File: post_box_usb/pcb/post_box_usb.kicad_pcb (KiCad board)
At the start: 4 copper layers, 92.9 x 45 mm, 114 parts, among them U1 MCP1700T-3302E/MB, U2 PMV65XP,215, X1 MC146 32768Hz

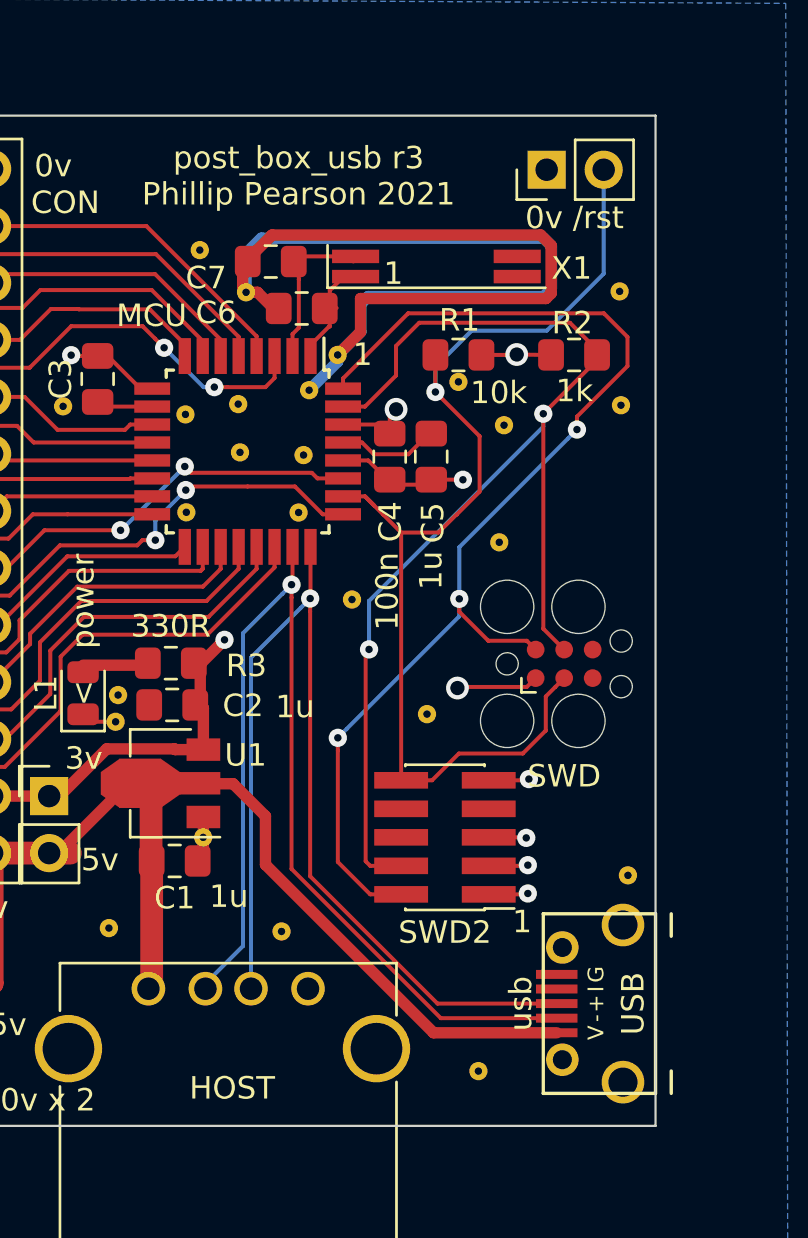
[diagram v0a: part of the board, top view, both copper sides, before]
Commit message: post_box_usb: Start r4; generate JLCPCB BOM so I can get them to assemble these.
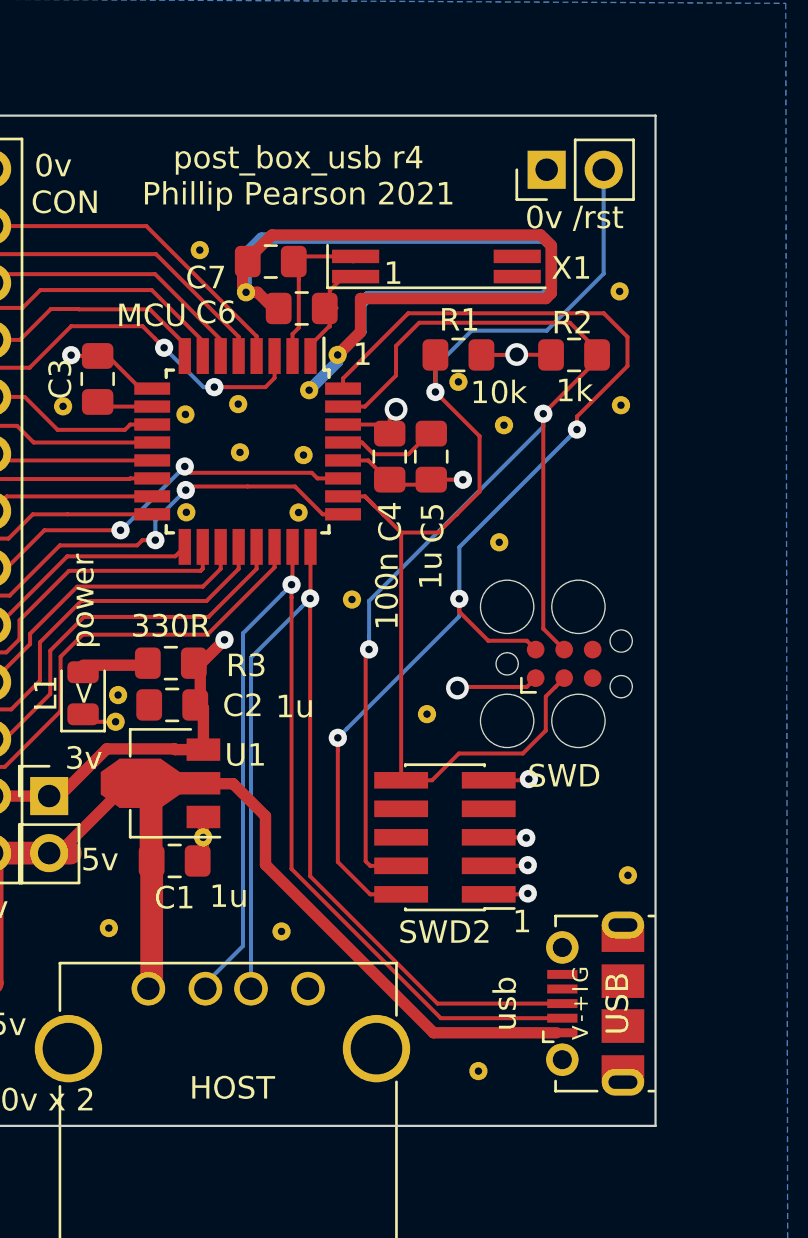
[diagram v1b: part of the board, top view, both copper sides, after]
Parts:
- C6, C7: value 15p -> NF 15p
- CON, FPGA_IO, FPGA_IO2, TEST: value pins -> NF pins
- FPGA_JTAG: value lattice jtag -> NF lattice jtag
- HOST: value usb host -> NF usb host
- PWR: value reset -> NF power
- R18, R19: value 0R NF -> NF 0R
- RST: value reset -> NF reset
- USB: footprint myelin-kicad:micro_usb_b_smd_molex -> Connector_USB:USB_Micro-B_Molex-105017-0001
- X1: value MC146 32768Hz -> NF MC146 32768Hz
- moved USB 0.69 mm to (197.3, 169.6)
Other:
- board text added: "post_box_usb r4 Copyright 2017-2021 Google Inc Designed by Phillip Pearson myelin.nz/acorn/postbox"
- board text added: "post_box_usb r4 Phillip Pearson 2021"
- board text removed: "post_box_usb r3 Copyright 2017-2021 Google Inc Designed by Phillip Pearson myelin.nz/acorn/postbox"
- board text removed: "post_box_usb r3 Phillip Pearson 2021"

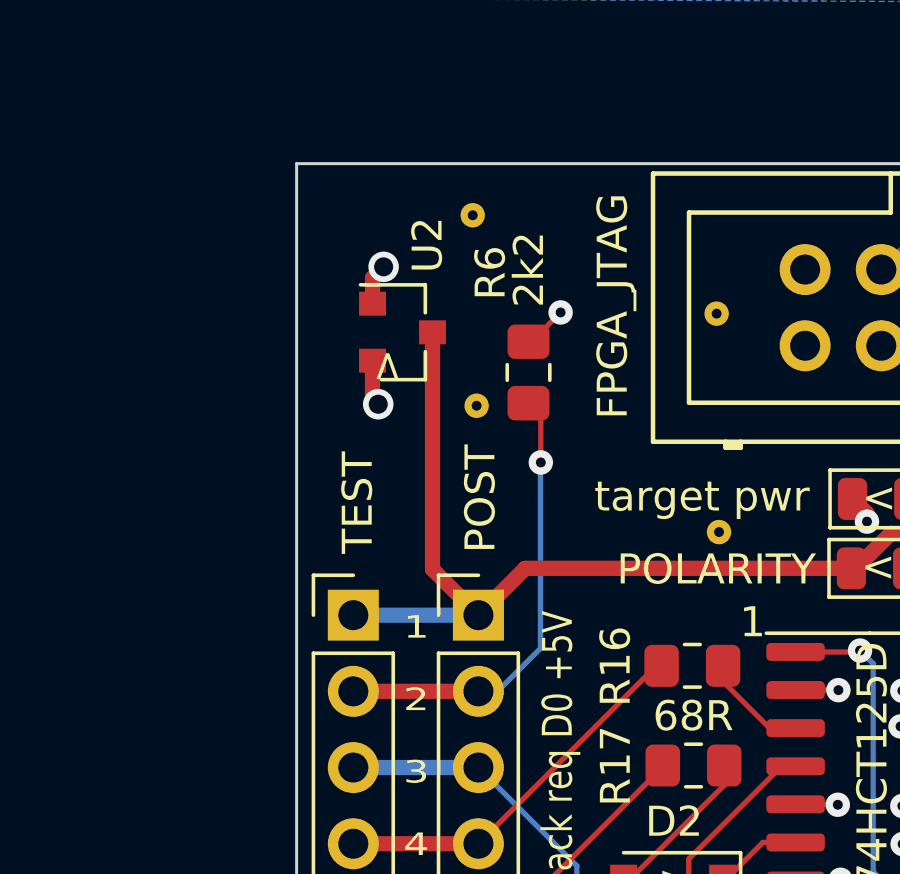
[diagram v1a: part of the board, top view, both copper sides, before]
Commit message: post_box_usb: add two pulldown resistors for target_5V_ext
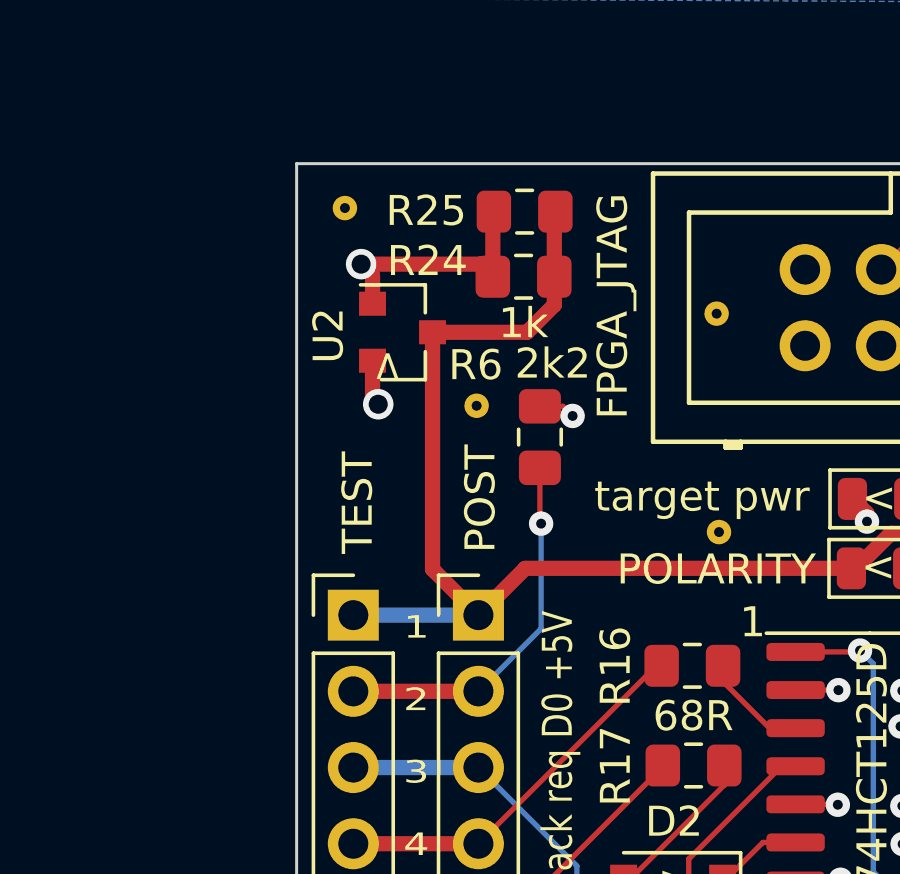
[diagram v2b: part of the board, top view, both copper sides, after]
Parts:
- added R24: 1k, Resistor_SMD:R_0805_2012Metric_Pad1.15x1.40mm_HandSolder, F.Cu at (114.7, 133.8)
- added R25: 1k, Resistor_SMD:R_0805_2012Metric_Pad1.15x1.40mm_HandSolder, F.Cu at (114.7, 131.6)
- moved staple_single25 4.27 mm to (108.7, 131.5)
- moved R6 2.19 mm to (115.2, 139.1)
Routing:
- net target_5V_ext: track 34.4 -> 42.1 mm
- net target_GND: track 24.2 -> 31.1 mm
- net target_D0: track 15.2 -> 12.5 mm
